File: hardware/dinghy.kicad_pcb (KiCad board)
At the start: 2 copper layers, 105.5 x 88.9 mm, 53 parts, among them J101 Fan 1, J102 Motor, J103 Endtemp, J104 PGM, J105 Power, J106 UART, J107 Header 1, J108 Header 2, J201 Fan2, Q101 IRLR7843PbF, Q102 IRLR7843PbF, Q201 IRLR7843PbF, SW101 SW_Push, U101 TMC2130, U102 ATMEGA1284P-AU, Y101 Crystal

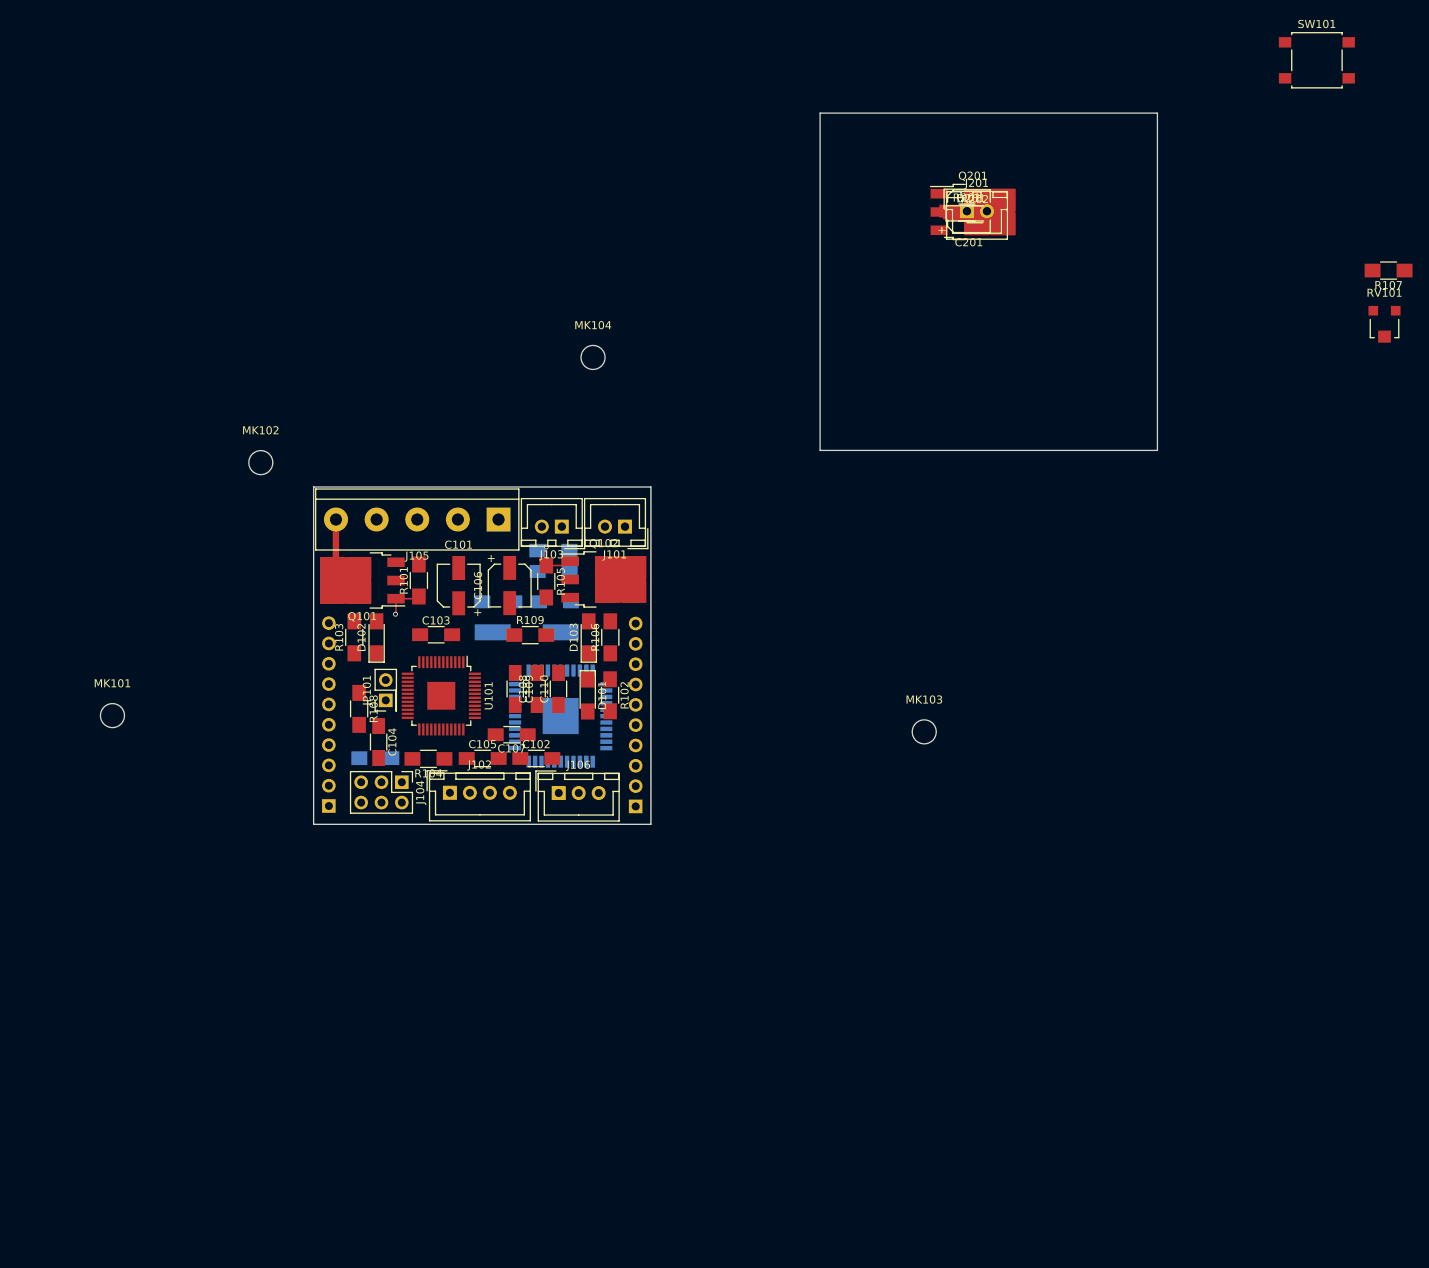
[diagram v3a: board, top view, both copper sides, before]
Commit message: Components positioned
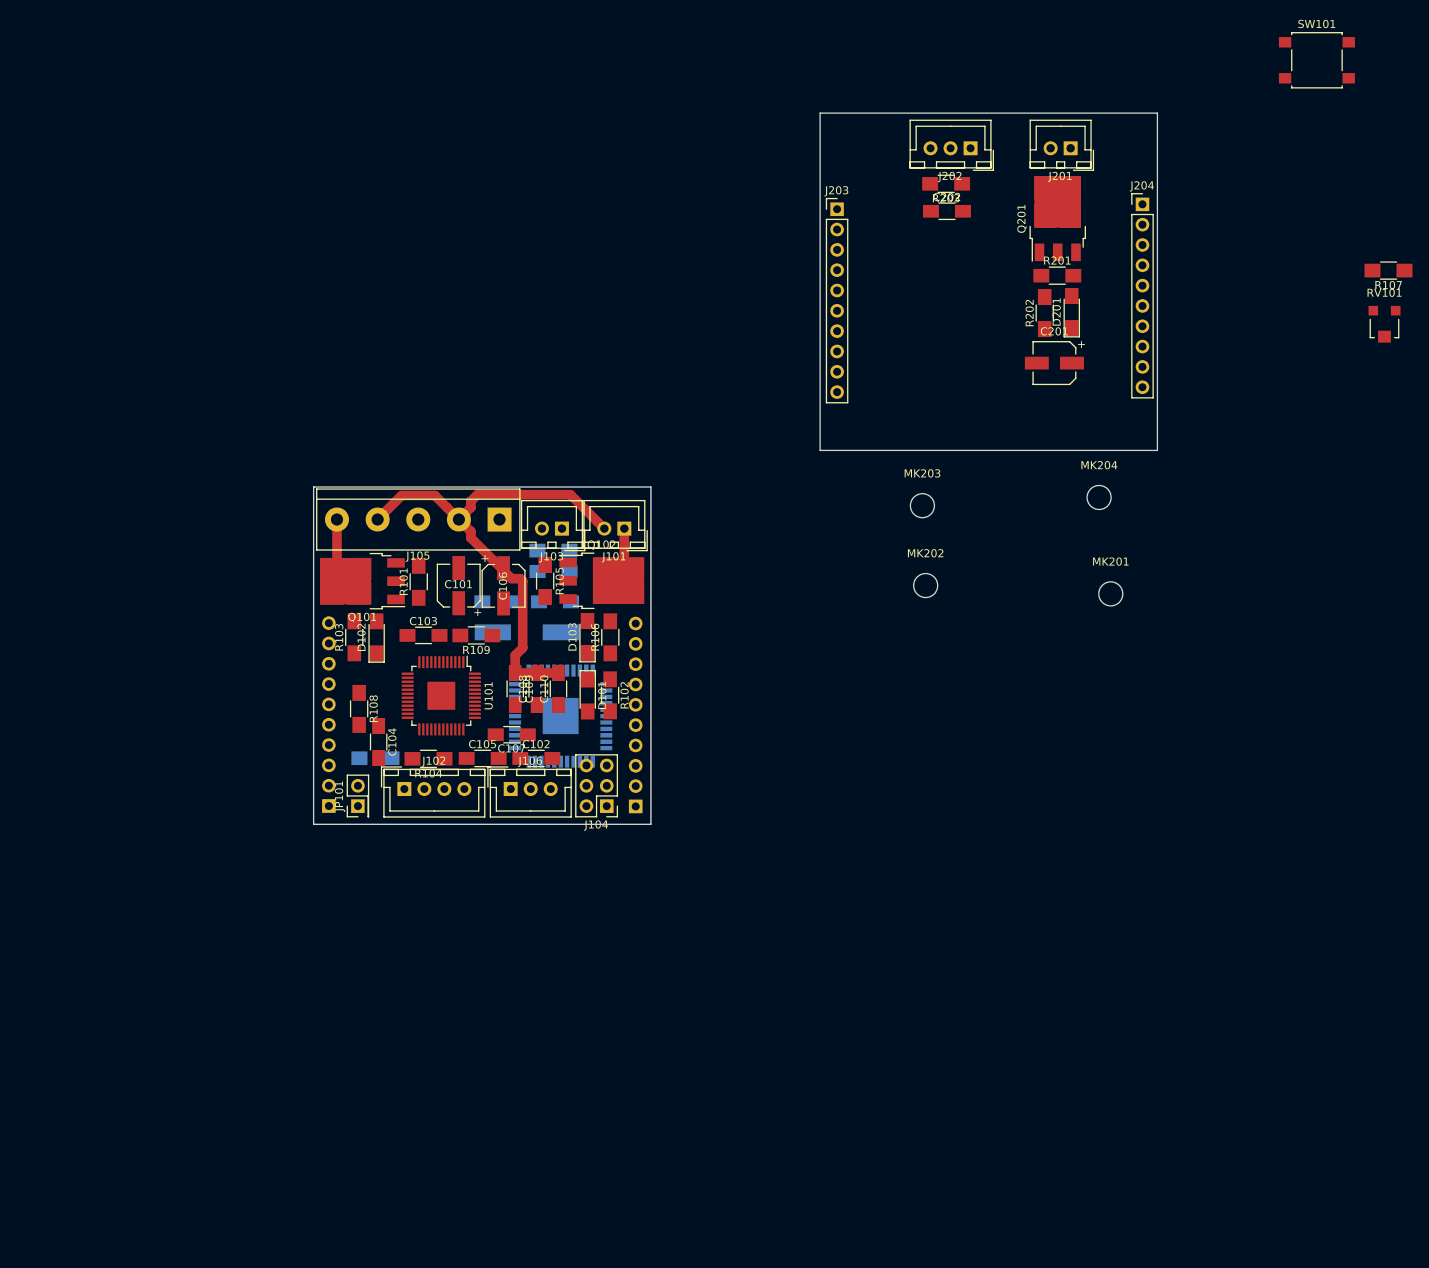
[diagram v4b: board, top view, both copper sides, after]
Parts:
- removed MK101, MK102, MK103, MK104: Mounting_Hole, Mounting_Holes:MountingHole_3mm
- added C202: 10µ, Capacitors_SMD:C_1206_HandSoldering, F.Cu at (203.6, 44.8)
- added J202: Endstop, Connectors_JST:JST_XH_B03B-XH-A_03x2.50mm_Straight, F.Cu at (206.6, 36.9)
- added J203: Conn_01x10_Female, Pin_Headers:Pin_Header_Straight_1x10_Pitch2.54mm, F.Cu at (189.9, 44.5)
- added J204: Conn_01x10_Female, Pin_Headers:Pin_Header_Straight_1x10_Pitch2.54mm, F.Cu at (228.1, 43.9)
- added MK201: Mounting_Hole, Mounting_Holes:MountingHole_3mm, F.Cu at (224.1, 92.6)
- added MK202: Mounting_Hole, Mounting_Holes:MountingHole_3mm, F.Cu at (201.0, 91.6)
- added MK203: Mounting_Hole, Mounting_Holes:MountingHole_3mm, F.Cu at (200.6, 81.6)
- added MK204: Mounting_Hole, Mounting_Holes:MountingHole_3mm, F.Cu at (222.6, 80.6)
- added R203: 10k, Resistors_SMD:R_1206_HandSoldering, F.Cu at (203.5, 41.4)
- moved J104 25.8 mm to (161.1, 119.1), turned to 180 degrees
- moved C201 21.8 mm to (217.1, 63.8), turned to 180 degrees
- moved D201 17.6 mm to (219.2, 57.4), turned to 90 degrees
- moved J201 15.2 mm to (219.1, 36.9), turned to 180 degrees
- moved R202 15.1 mm to (215.8, 57.5), turned to 90 degrees
- moved R201 13.8 mm to (217.4, 52.8)
- moved JP101 13.7 mm to (130.0, 119.1)
- moved Q201 10.6 mm to (217.5, 45.7), turned to 90 degrees
- moved R109 6.74 mm to (144.8, 97.8), turned to 180 degrees
- moved J106 6.02 mm to (149.1, 117.0)
- moved J102 5.72 mm to (135.8, 117.0)
- moved C103 1.58 mm to (138.2, 97.8)
- moved C106 0.77 mm to (148.2, 91.6)
- moved Q102 0.30 mm to (160.5, 91.0)
- moved J101 0.26 mm to (163.3, 84.5)
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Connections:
- net Net-(J101-Pad1) renamed /FAN-GND
- J105 pad 5: /HOTEND- -> (no net)
- Q101 pad 2: /HOTEND- -> /HOTEND-GND
- R103 pad 2: /HOTEND- -> /HOTEND-GND
- U101 pad 11: (no net) -> GND
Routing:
- net VMot: track 0.00 -> 63.8 mm
- net /HOTEND-GND: track 0.00 -> 6.43 mm
- net /HOTEND-: track 6.29 -> 0.00 mm
- net /FAN1: track 5.52 -> 0.00 mm, vias 1 -> 0
- net /FAN-GND: track 0.00 -> 5.39 mm
- net /HOTEND: track 4.94 -> 0.00 mm, vias 1 -> 0
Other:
- net class Default: clearance 0.3 -> 0.254; trace_width 0.8 -> 0.254; via_dia 0.6 -> 0.6858; via_drill 0.4 -> 0.3302
- net class Digital removed
- net class PW12 added: clearance 1, trace_width 1.2, via_dia 0.6858, via_drill 0.3302
- net class PW12++ added: clearance 1, trace_width 1.2, via_dia 0.6858, via_drill 0.3302
- net class PW5 added: clearance 0.254, trace_width 0.254, via_dia 0.6858, via_drill 0.3302
- net class Power removed
- net class Signal added: clearance 0.254, trace_width 0.254, via_dia 0.6858, via_drill 0.3302
- rule trace_clearance: 0.3 -> 0.254
- rule trace_min: 0.2 -> 0.1524
- rule via_min_drill: 0.3 -> 0.254
- rule via_min_size: 0.4 -> 0.508

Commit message: Top layer routet
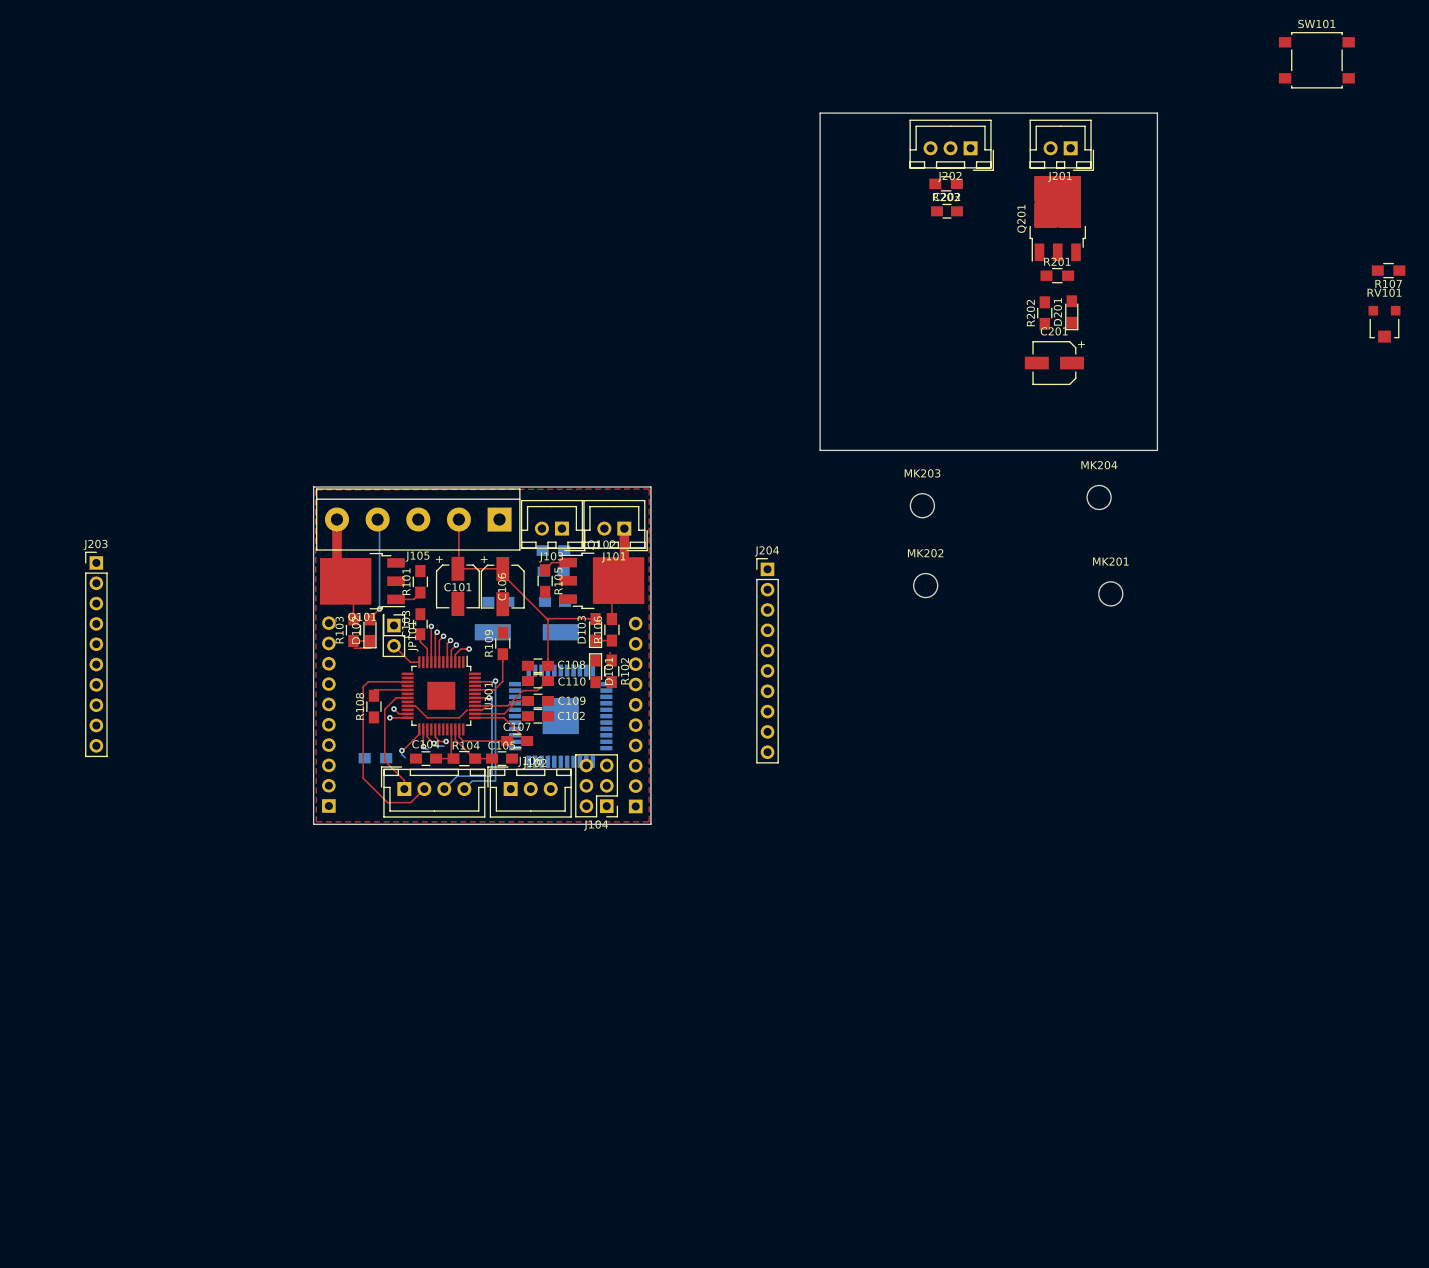
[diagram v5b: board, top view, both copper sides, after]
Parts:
- C102, C103, C104, C105, C107, C108, C109, C110, C111, C112, C113, C202: footprint Capacitors_SMD:C_1206_HandSoldering -> Capacitors_SMD:C_0805_HandSoldering
- D101, D102, D103, D201: footprint LEDs:LED_1206_HandSoldering -> LEDs:LED_0805_HandSoldering
- R101, R102, R103, R104, R105, R106, R107, R108, R109, R110, R111, R201, R202, R203: footprint Resistors_SMD:R_1206_HandSoldering -> Resistors_SMD:R_0805_HandSoldering
- moved J203 102.6 mm to (97.3, 88.7)
- moved J204 65.4 mm to (181.2, 89.5)
- moved JP101 23.0 mm to (134.5, 96.6), turned to 270 degrees
- moved C104 6.27 mm to (138.5, 113.2), turned to 0 degrees
- moved C102 5.29 mm to (152.5, 107.9)
- moved R104 4.49 mm to (143.3, 113.2)
- moved R109 3.45 mm to (148.1, 98.8), turned to 90 degrees
- moved C109 3.22 mm to (152.5, 106.0), turned to 180 degrees
- moved D101 3.16 mm to (159.7, 102.3)
- moved R102 3.01 mm to (161.7, 102.3)
- moved C108 2.90 mm to (152.5, 101.6), turned to 0 degrees
- moved C110 2.75 mm to (152.5, 103.5), turned to 0 degrees
- moved C105 2.41 mm to (148.0, 113.2)
- moved R108 1.87 mm to (132.0, 106.7), turned to 90 degrees
- moved C103 1.46 mm to (137.8, 96.4), turned to 90 degrees
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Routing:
- net /OB1: track 0.00 -> 26.9 mm
- net /OA1: track 0.00 -> 19.4 mm, vias 0 -> 1
- net /OA2: track 0.00 -> 18.2 mm, vias 0 -> 1
- net /OB2: track 0.00 -> 14.4 mm
- net +5V: track 0.00 -> 9.83 mm
- net Net-(C107-Pad2): track 0.00 -> 7.80 mm
- net Net-(R109-Pad1): track 0.00 -> 7.31 mm
- net Net-(C109-Pad2): track 0.00 -> 7.29 mm
- net Net-(C107-Pad1): track 0.00 -> 7.14 mm
- net Net-(C105-Pad1): track 0.00 -> 6.84 mm
- net Net-(R108-Pad1): track 0.00 -> 4.69 mm
- net /M-DCIN: track 0.00 -> 4.67 mm, vias 0 -> 1
- net /FAN-GND: track 5.39 -> 9.90 mm
- net /M-DIR: track 0.00 -> 4.49 mm, vias 0 -> 1
- net /HOTEND-GND: track 6.43 -> 10.8 mm
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- added copper zone on F.Cu, net GND
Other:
- net class Default: clearance 0.254 -> 0.2; trace_width 0.254 -> 0.2
- net class PW12 removed
- net class PW12++ removed
- net class PW5 removed
- net class Signal removed
- rule trace_clearance: 0.254 -> 0.2
